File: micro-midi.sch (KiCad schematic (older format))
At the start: 6 parts

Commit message: add footprints first try and create ratsnest
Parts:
- D1: renamed from D?; footprint Diode_THT:D_DO-35_SOD27_P7.62mm_Horizontal -> Diode_SMD:D_1206_3216Metric
- J1: renamed from J?; footprint (none) -> Connector_Audio:Jack_3.5mm_QingPu_WQP-PJ398SM_Vertical_CircularHoles
- J2: renamed from J?; footprint (none) -> Connector_PinHeader_2.54mm:PinHeader_1x03_P2.54mm_Vertical
- R1: footprint (none) -> Resistor_SMD:R_1206_3216Metric
- R2: renamed from R?; footprint (none) -> Resistor_SMD:R_1206_3216Metric
- gave numbers to parts that had none: 1
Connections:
- wire segments 27 -> 24
- no-connect marks 0 -> 2
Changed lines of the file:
@@
 $EndDescr
 $Comp
-L Connector:AudioJack3 J?
+L Connector:AudioJack3 J1
 U 1 1 5E7D1AF1
 P 2950 2900
-F 0 "J?" H 2671 2833 50  0000 R CNN
+F 0 "J1" H 2671 2833 50  0000 R CNN
 F 1 "AudioJack3" H 2671 2924 50  0000 R CNN
-F 2 "" H 2950 2900 50  0001 C CNN
+F 2 "Connector_Audio:Jack_3.5mm_QingPu_WQP-PJ398SM_Vertical_CircularHoles" H 2950 2900 50  0001 C CNN
 F 3 "~" H 2950 2900 50  0001 C CNN
 	1    2950 2900
@@
 F 0 "R1" H 5880 2354 50  0000 R CNN
 F 1 "10K" H 5880 2445 50  0000 R CNN
-F 2 "" V 5880 2400 50  0001 C CNN
+F 2 "Resistor_SMD:R_1206_3216Metric" V 5880 2400 50  0001 C CNN
 F 3 "~" H 5950 2400 50  0001 C CNN
 	1    5950 2400
@@
 $EndComp
 $Comp
-L Device:R R?
+L Device:R R2
 U 1 1 5E7D6E0A
 P 4150 2800
-F 0 "R?" V 3943 2800 50  0000 C CNN
+F 0 "R2" V 3943 2800 50  0000 C CNN
 F 1 "220R" V 4034 2800 50  0000 C CNN
-F 2 "" V 4080 2800 50  0001 C CNN
+F 2 "Resistor_SMD:R_1206_3216Metric" V 4080 2800 50  0001 C CNN
 F 3 "~" H 4150 2800 50  0001 C CNN
 	1    4150 2800
@@
 $EndComp
 $Comp
-L power:+5V #PWR?
+L power:+5V #PWR01
 U 1 1 5E7D8E69
 P 5600 1150
-F 0 "#PWR?" H 5600 1000 50  0001 C CNN
+F 0 "#PWR01" H 5600 1000 50  0001 C CNN
 F 1 "+5V" H 5615 1323 50  0000 C CNN
 F 2 "" H 5600 1150 50  0001 C CNN
@@
 $EndComp
 $Comp
-L power:GND #PWR?
+L power:GND #PWR02
 U 1 1 5E7D92E0
 P 5600 4100
-F 0 "#PWR?" H 5600 3850 50  0001 C CNN
+F 0 "#PWR02" H 5600 3850 50  0001 C CNN
 F 1 "GND" H 5605 3927 50  0000 C CNN
 F 2 "" H 5600 4100 50  0001 C CNN
@@
 $EndComp
 $Comp
-L Connector:Conn_01x03_Male J?
+L Connector:Conn_01x03_Male J2
 U 1 1 5E7D9F51
-P 7800 2900
-F 0 "J?" H 7772 2832 50  0000 R CNN
-F 1 "Conn_01x03_Male" H 7772 2923 50  0000 R CNN
-F 2 "" H 7800 2900 50  0001 C CNN
-F 3 "~" H 7800 2900 50  0001 C CNN
-	1    7800 2900
+P 7800 2800
+F 0 "J2" H 7772 2732 50  0000 R CNN
+F 1 "Conn_01x03_Male" H 7772 2823 50  0000 R CNN
+F 2 "Connector_PinHeader_2.54mm:PinHeader_1x03_P2.54mm_Vertical" H 7800 2800 50  0001 C CNN
+F 3 "~" H 7800 2800 50  0001 C CNN
+	1    7800 2800
 	-1   0    0    1
 $EndComp
 $Comp
-L Isolator:6N137 U?
+L Isolator:6N137 U1
 U 1 1 5E7DA516
 P 5000 2800
-F 0 "U?" H 5000 3267 50  0000 C CNN
+F 0 "U1" H 5000 3267 50  0000 C CNN
 F 1 "6N137" H 5000 3176 50  0000 C CNN
 F 2 "Package_DIP:DIP-8_W7.62mm" H 5000 2300 50  0001 C CNN
@@
 	5600 3000 5300 3000
 Wire Wire Line
-	7600 2800 6800 2800
-Wire Wire Line
-	6800 2800 6800 1950
+	7600 2700 6800 2700
 Wire Wire Line
 	6800 1950 5950 1950
@@
 	5600 1950 5600 2600
 Wire Wire Line
-	7600 3000 6800 3000
+	7600 2900 6800 2900
 Wire Wire Line
-	6800 3000 6800 3350
-Wire Wire Line
-	6800 3350 5600 3350
-Connection ~ 5600 3350
-Wire Wire Line
-	5600 3350 5600 3000
+	6800 2900 6800 3000
 Wire Wire Line
 	5300 2800 5950 2800
-Wire Wire Line
-	6600 2800 6600 2900
-Wire Wire Line
-	6600 2900 7600 2900
 Wire Wire Line
 	5950 2250 5950 1950
@@
 	5950 2550 5950 2800
 Connection ~ 5950 2800
-Wire Wire Line
-	5950 2800 6600 2800
 $Comp
-L Diode:1N4148 D?
+L Diode:1N4148 D1
 U 1 1 5E7E1942
 P 4450 2950
-F 0 "D?" V 4404 3029 50  0000 L CNN
+F 0 "D1" V 4404 3029 50  0000 L CNN
 F 1 "1N4148" V 4495 3029 50  0000 L CNN
-F 2 "Diode_THT:D_DO-35_SOD27_P7.62mm_Horizontal" H 4450 2775 50  0001 C CNN
+F 2 "Diode_SMD:D_1206_3216Metric" H 4450 2775 50  0001 C CNN
 F 3 "https://assets.nexperia.com/documents/data-sheet/1N4148_1N4448.pdf" H 4450 2950 50  0001 C CNN
 	1    4450 2950
@@
 	3800 2900 3150 2900
 Connection ~ 4450 3100
+NoConn ~ 5300 2700
+NoConn ~ 3150 3000
 Wire Wire Line
-	5600 3350 5600 4100
+	6800 2700 6800 1950
+Wire Wire Line
+	5600 3000 5600 4100
+Wire Wire Line
+	5600 3000 6800 3000
+Connection ~ 5600 3000
+Wire Wire Line
+	5950 2800 7600 2800
 $EndSCHEMATC

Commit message: add midi-out and activity leds
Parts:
- removed J2: Conn_01x03_Male, Connector_PinHeader_2.54mm:PinHeader_1x03_P2.54mm_Vertical, symbol Connector:Conn_01x03_Male
- added D2, D3: LED, symbol Device:LED
- added J2: Conn_01x04_Male, symbol Connector:Conn_01x04_Male
- added J3, J4: AudioJack3, Connector_Audio:Jack_3.5mm_QingPu_WQP-PJ398SM_Vertical_CircularHoles, symbol Connector:AudioJack3
- added R3, R4: 470, symbol Device:R
- added U1: 74HC04, symbol 74xx:74HC04
- added U3: 74AHC04, symbol 74xx:74AHC04
- renumbered R2 to R1, R1 to R2, U1 to U2
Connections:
- wire segments 24 -> 59
- no-connect marks 2 -> 4

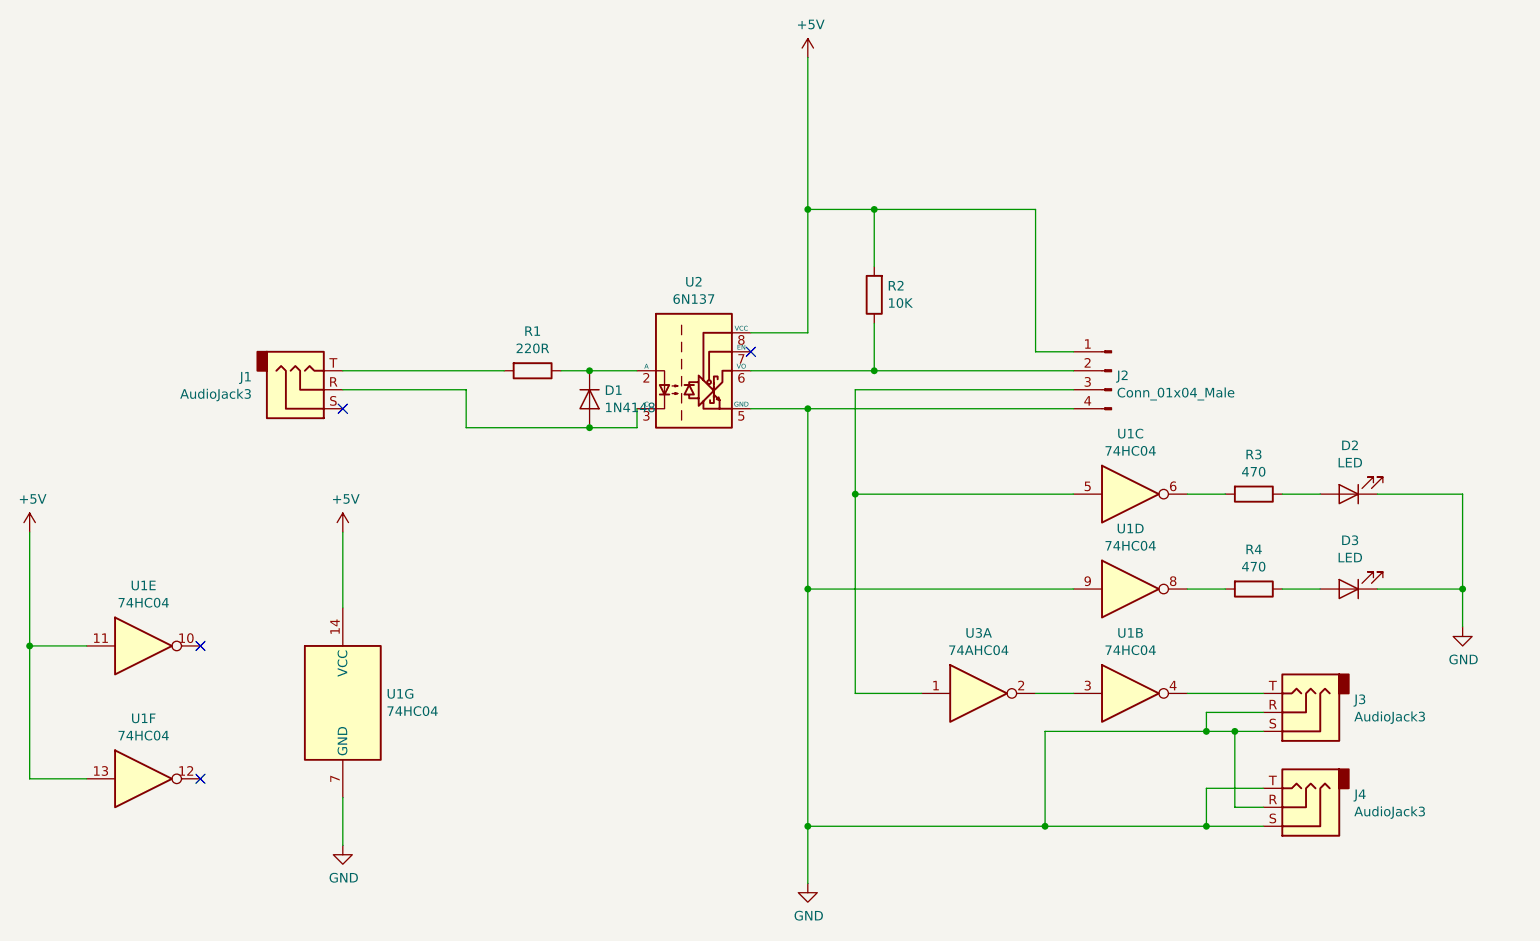
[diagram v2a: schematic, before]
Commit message: add power flags to fix errors
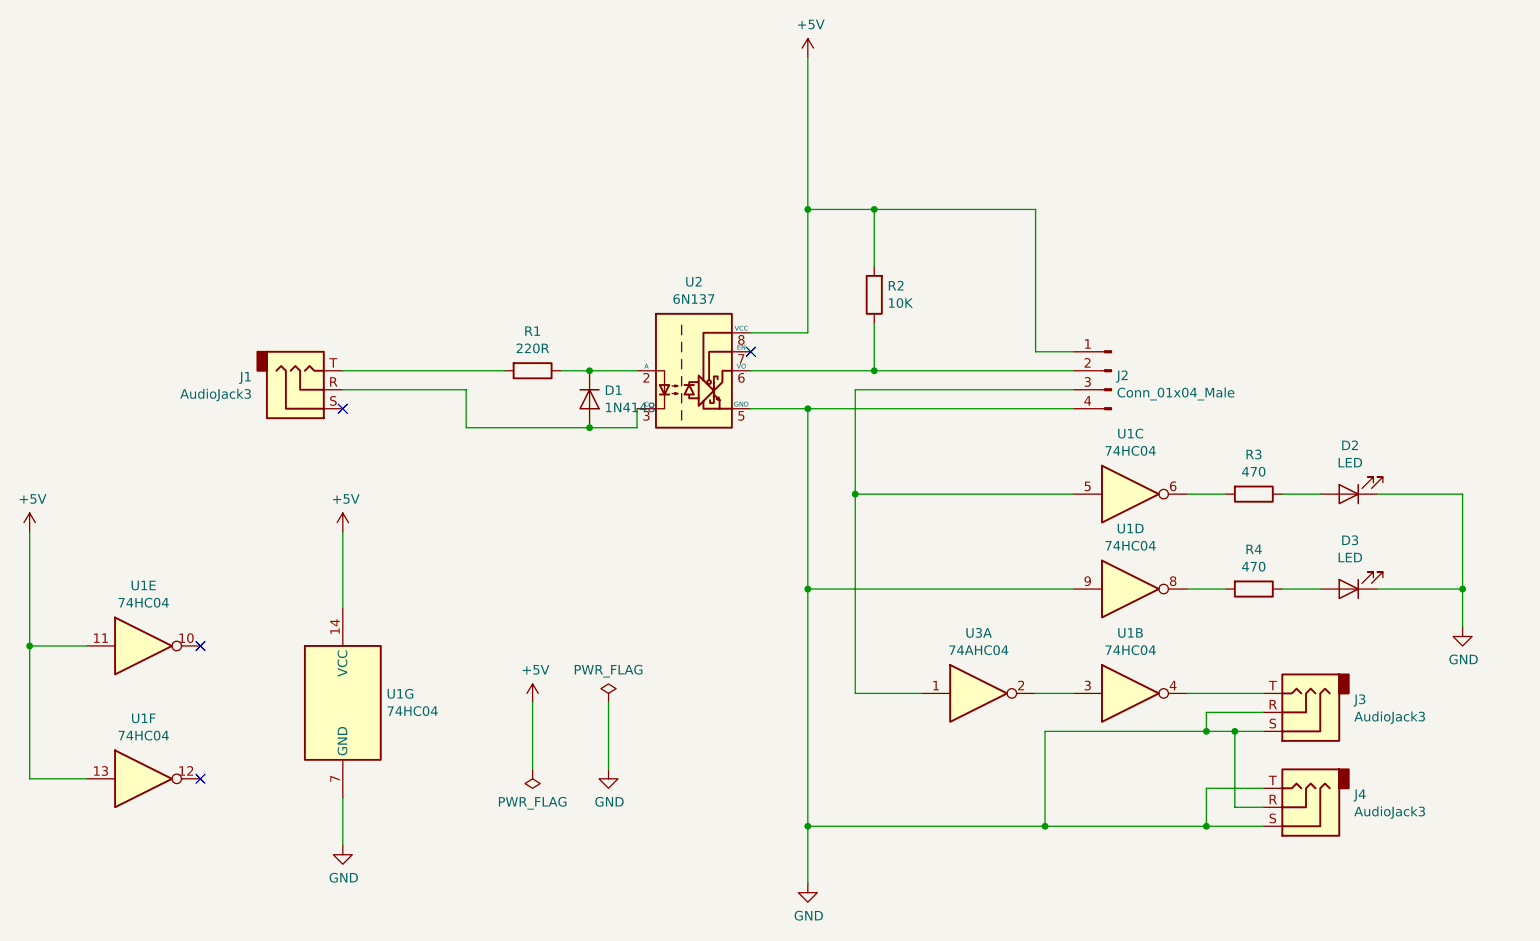
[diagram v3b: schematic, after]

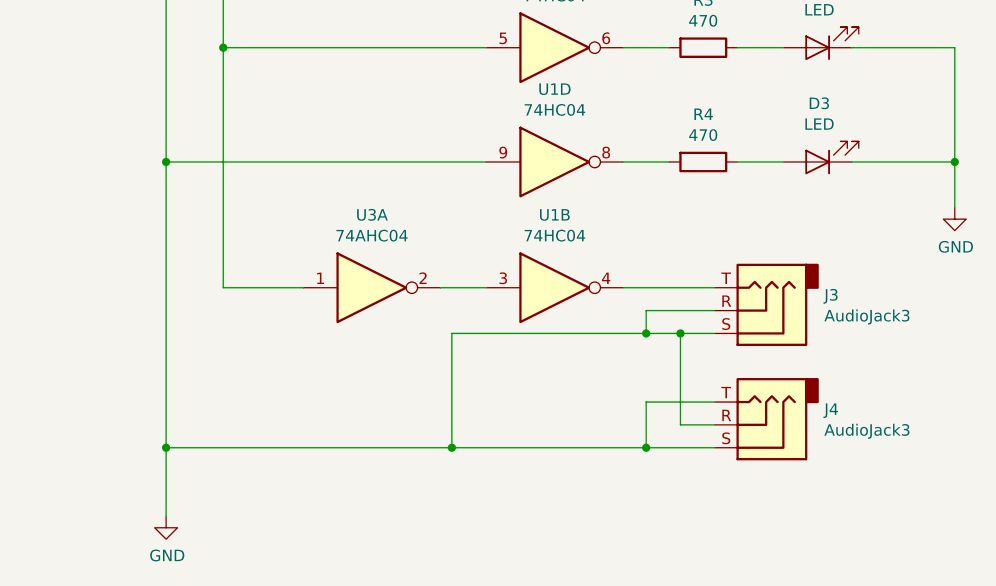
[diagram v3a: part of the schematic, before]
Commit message: remove midi thru
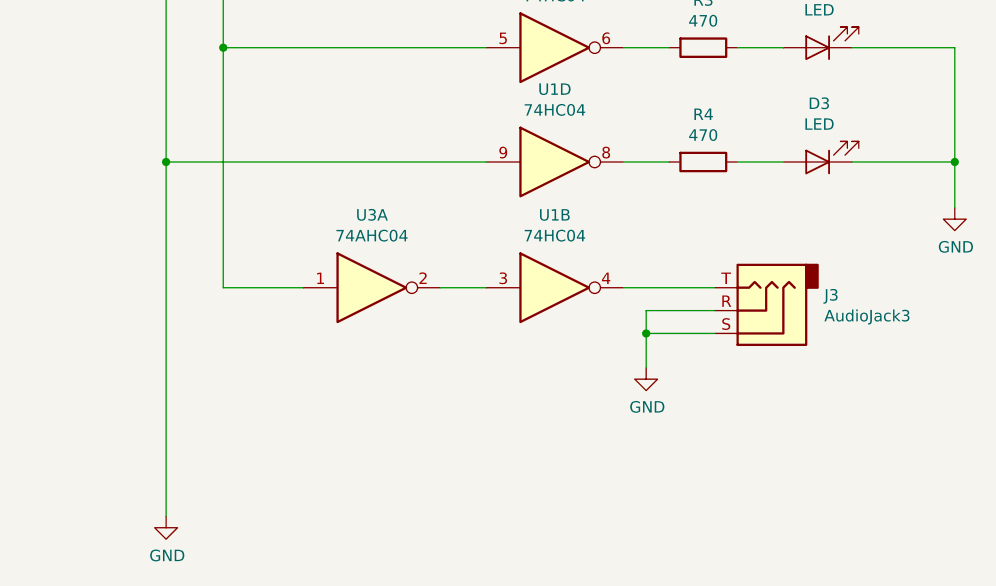
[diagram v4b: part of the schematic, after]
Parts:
- removed J4: AudioJack3, Connector_Audio:Jack_3.5mm_QingPu_WQP-PJ398SM_Vertical_CircularHoles, symbol Connector:AudioJack3
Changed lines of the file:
@@
-	-1   0    0    1
-$EndComp
-$Comp
-L Connector:AudioJack3 J4
-U 1 1 5E82CC92
-P 8200 5100
-F 0 "J4" H 7921 5033 50  0000 R CNN
-F 1 "AudioJack3" H 7921 5124 50  0000 R CNN
-F 2 "Connector_Audio:Jack_3.5mm_QingPu_WQP-PJ398SM_Vertical_CircularHoles" H 8200 5100 50  0001 C CNN
-F 3 "~" H 8200 5100 50  0001 C CNN
-	1    8200 5100
 	-1   0    0    1
 $EndComp
 Wire Wire Line
 	7700 4600 7700 4700
-Connection ~ 7700 4700
-Wire Wire Line
-	7700 4700 6850 4700
 Wire Wire Line
 	8000 4600 7700 4600
-Wire Wire Line
-	7850 4700 7700 4700
-Wire Wire Line
-	8000 4700 7850 4700
-Connection ~ 7850 4700
-Wire Wire Line
-	7850 5100 7850 4700
-Wire Wire Line
-	8000 5100 7850 5100
-Wire Wire Line
-	7700 5000 7700 5200
-Wire Wire Line
-	8000 5000 7700 5000
-Wire Wire Line
-	8000 5200 7700 5200
-Wire Wire Line
-	6850 4700 6850 5200
-Connection ~ 7700 5200
-Wire Wire Line
-	7700 5200 6850 5200
 Connection ~ 5600 3950
 $Comp
@@
 $EndComp
 Wire Wire Line
-	5600 3950 5600 5200
-Wire Wire Line
-	6850 5200 5600 5200
-Wire Wire Line
 	5950 1950 6800 1950
-Connection ~ 6850 5200
-Connection ~ 5600 5200
-Wire Wire Line
-	5600 5200 5600 5500
 Wire Wire Line
 	4550 4550 4550 4900
 Wire Wire Line
 	4150 4550 4150 4900
+Wire Wire Line
+	5600 3950 5600 5500
+Wire Wire Line
+	7700 4700 8000 4700
+$Comp
+L power:GND #PWR?
+U 1 1 5EA4A4EF
+P 7700 4850
+F 0 "#PWR?" H 7700 4600 50  0001 C CNN
+F 1 "GND" H 7705 4677 50  0000 C CNN
+F 2 "" H 7700 4850 50  0001 C CNN
+F 3 "" H 7700 4850 50  0001 C CNN
+	1    7700 4850
+	1    0    0    -1
+$EndComp
+Wire Wire Line
+	7700 4700 7700 4850
+Connection ~ 7700 4700
 $EndSCHEMATC

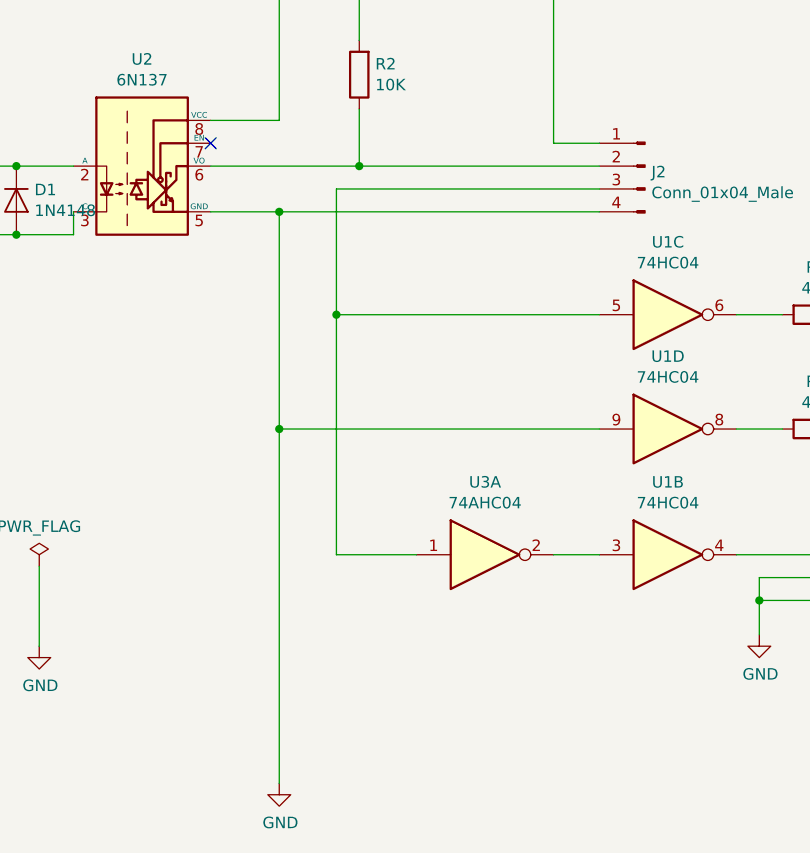
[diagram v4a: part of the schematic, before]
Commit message: fix midi out led and ground
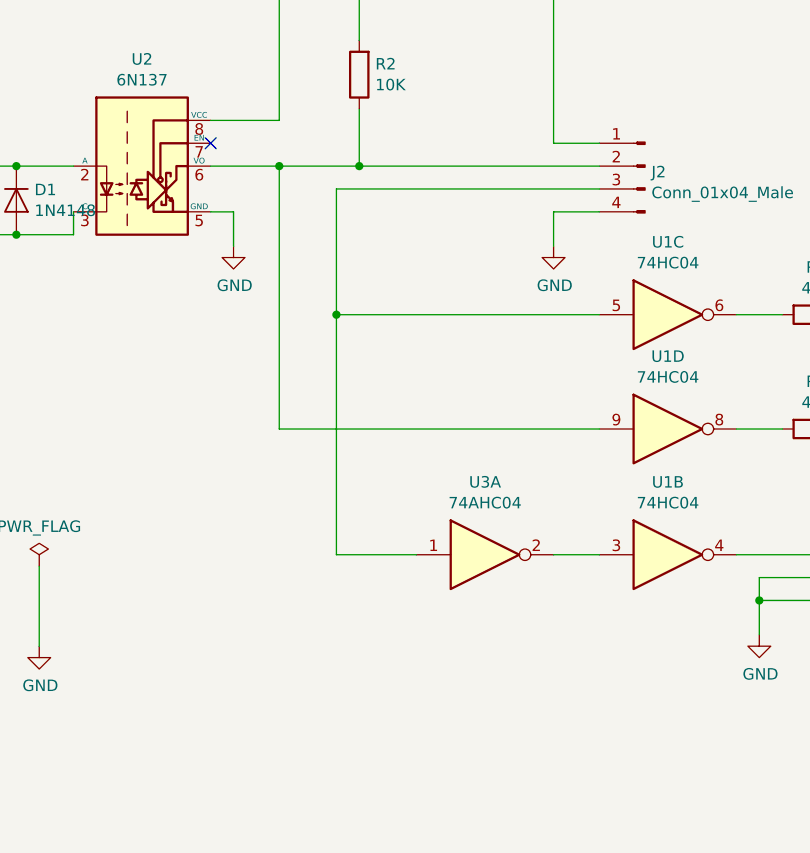
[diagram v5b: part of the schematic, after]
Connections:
- net GND: no longer U1.9
- net at J2.2 (Pin_2), R2.1, U2.6 (VO): now also U1.9
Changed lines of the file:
@@
 	5600 1950 5600 2600
 Wire Wire Line
-	5300 2800 5950 2800
+	5300 2800 5600 2800
 Wire Wire Line
 	5950 2250 5950 1950
@@
 	5850 2900 5850 3450
 Wire Wire Line
-	5600 3000 5600 3950
-Wire Wire Line
-	5300 3000 5600 3000
-Connection ~ 5600 3000
-Wire Wire Line
-	5600 3000 7000 3000
+	5300 3000 5400 3000
 $Comp
 L Device:R R3
@@
 Wire Wire Line
 	8000 4600 7700 4600
-Connection ~ 5600 3950
 $Comp
 L power:GND #PWR05
 U 1 1 5E7D92E0
-P 5600 5500
-F 0 "#PWR05" H 5600 5250 50  0001 C CNN
-F 1 "GND" H 5605 5327 50  0000 C CNN
-F 2 "" H 5600 5500 50  0001 C CNN
-F 3 "" H 5600 5500 50  0001 C CNN
-	1    5600 5500
+P 5400 3150
+F 0 "#PWR05" H 5400 2900 50  0001 C CNN
+F 1 "GND" H 5405 2977 50  0000 C CNN
+F 2 "" H 5400 3150 50  0001 C CNN
+F 3 "" H 5400 3150 50  0001 C CNN
+	1    5400 3150
 	1    0    0    -1
 $EndComp
@@
 	4150 4550 4150 4900
 Wire Wire Line
-	5600 3950 5600 5500
-Wire Wire Line
 	7700 4700 8000 4700
 $Comp
@@
 	7700 4700 7700 4850
 Connection ~ 7700 4700
+Wire Wire Line
+	5400 3000 5400 3150
+$Comp
+L power:GND #PWR?
+U 1 1 5EA55A66
+P 6800 3150
+F 0 "#PWR?" H 6800 2900 50  0001 C CNN
+F 1 "GND" H 6805 2977 50  0000 C CNN
+F 2 "" H 6800 3150 50  0001 C CNN
+F 3 "" H 6800 3150 50  0001 C CNN
+	1    6800 3150
+	1    0    0    -1
+$EndComp
+Wire Wire Line
+	7000 3000 6800 3000
+Wire Wire Line
+	6800 3000 6800 3150
+Connection ~ 5600 2800
+Wire Wire Line
+	5600 2800 5950 2800
+Wire Wire Line
+	5600 2800 5600 3950
 $EndSCHEMATC
